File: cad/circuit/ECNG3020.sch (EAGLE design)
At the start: 30 parts, among them Q1 16Mhz, T1 2N3904, T2 2N3904, T3 2N3904, T4 2N3904, T5 2N3904, U1 ATMEGA328P-PU, X1 22-23-2021, X2 22-23-2021, X3 22-23-2021, X4 22-23-2021, X5 22-23-2021, X6 22-23-2021, X7 22-23-2021

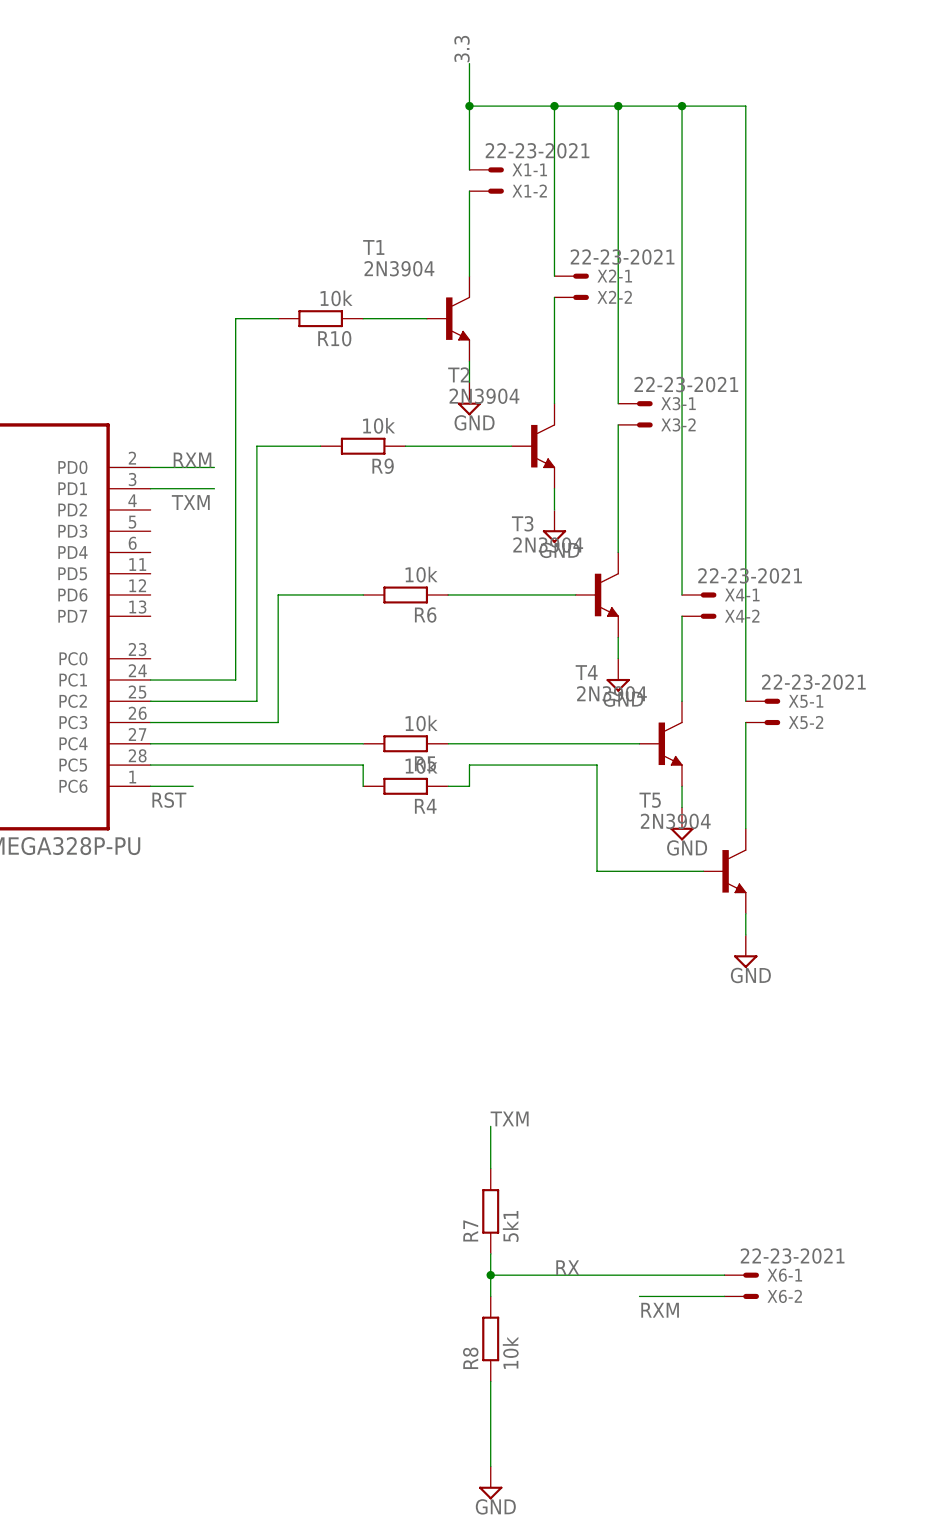
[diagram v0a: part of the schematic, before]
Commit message: Updated the PCB to use I2C instead of UART
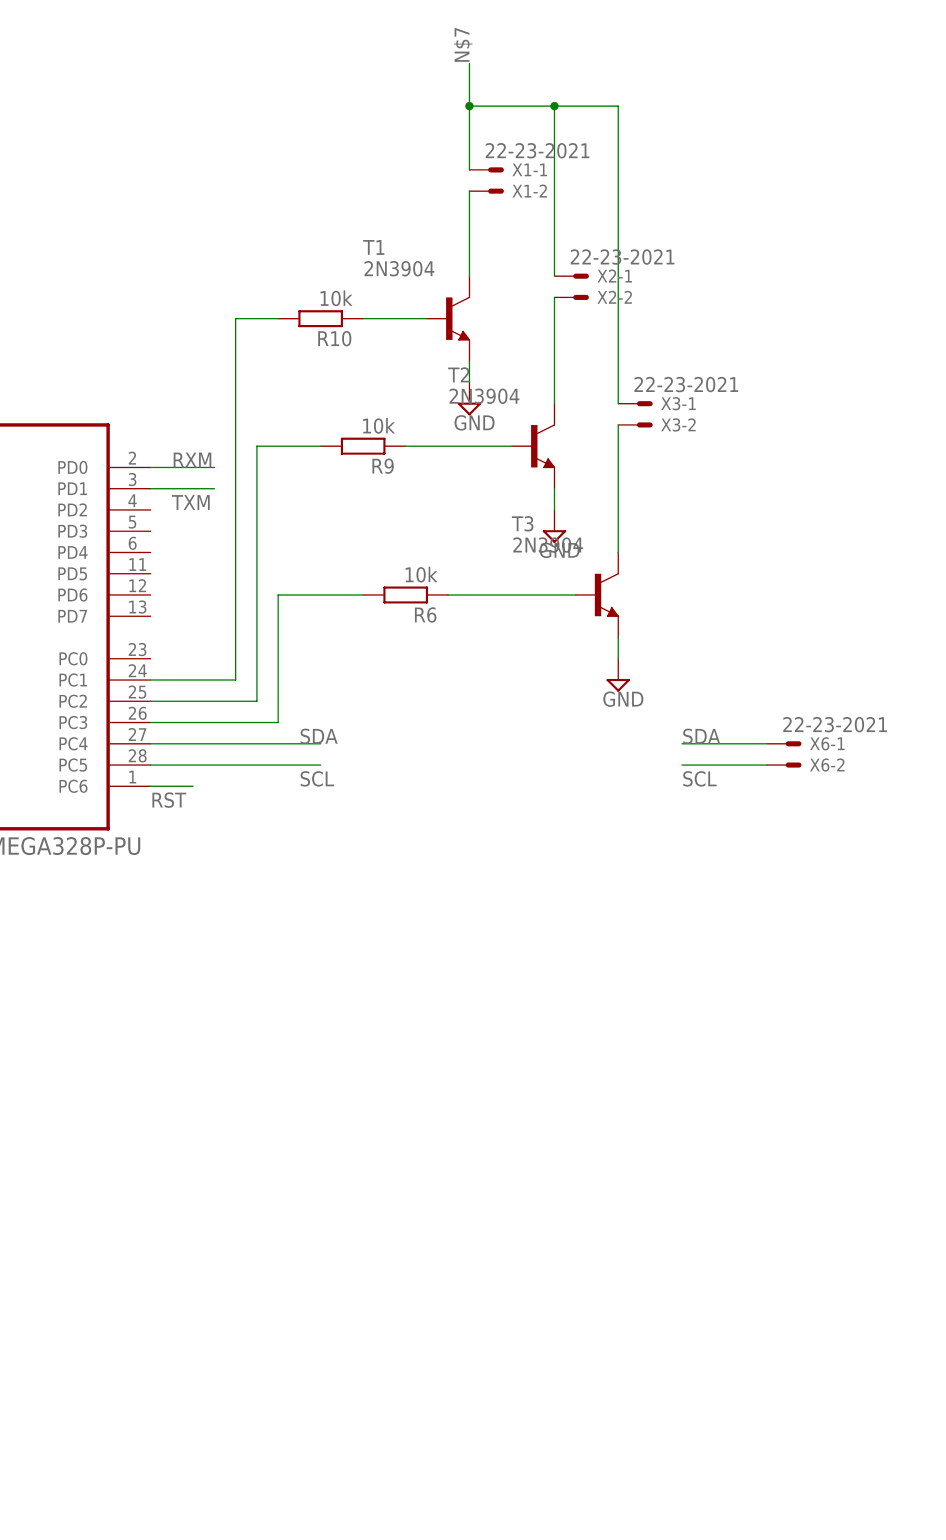
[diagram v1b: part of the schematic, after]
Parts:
- removed R4, R5, R8: 10k, rcl:R-EU_0207/10
- removed R7: 5k1, rcl:R-EU_0207/10
- removed T4, T5: 2N3904, transistor-neu-to92:2N3904
- removed X4, X5: 22-23-2021, con-molex:22-23-2021
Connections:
- removed net N$16: R5.1, T4.B
- removed net N$17: R5.2, U1.PC4
- removed net N$18: R4.2, U1.PC5
- removed net N$8: T5.C, X5-2.S
- removed net N$9: T4.C, X4-2.S
- removed net RX: R7.1, R8.2, X6-1.S
- new net SCL: U1.PC5, X6-2.S
- new net SDA: U1.PC4, X6-1.S
- net 3.3: no longer X1-1.S, X2-1.S, X3-1.S, X4-1.S, X5-1.S
- net GND: no longer R8.1, T4.E, T5.E
- net N$7: now also X1-1.S, X2-1.S, X3-1.S; no longer R4.1, T5.B
- net RXM: no longer X6-2.S
- net TXM: no longer R7.2
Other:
- moved on the sheet: X6-1, X6-2

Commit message: Updated the schematic and board
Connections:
- removed net RXM: U1.PD0
- removed net TXM: U1.PD1
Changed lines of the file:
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@@
-</segment>
-</net>
-<net name="TXM" class="0">
-<segment>
-<pinref part="U1" gate="A" pin="PD1"/>
-<wire x1="50.8" y1="104.14" x2="58.42" y2="104.14" width="0.1524" layer="91"/>
-<label x="53.34" y="101.6" size="1.778" layer="95"/>
-</segment>
-</net>
-<net name="RXM" class="0">
-<segment>
-<pinref part="U1" gate="A" pin="PD0"/>
-<wire x1="50.8" y1="106.68" x2="58.42" y2="106.68" width="0.1524" layer="91"/>
-<label x="53.34" y="106.68" size="1.778" layer="95"/>
 </segment>
 </net>

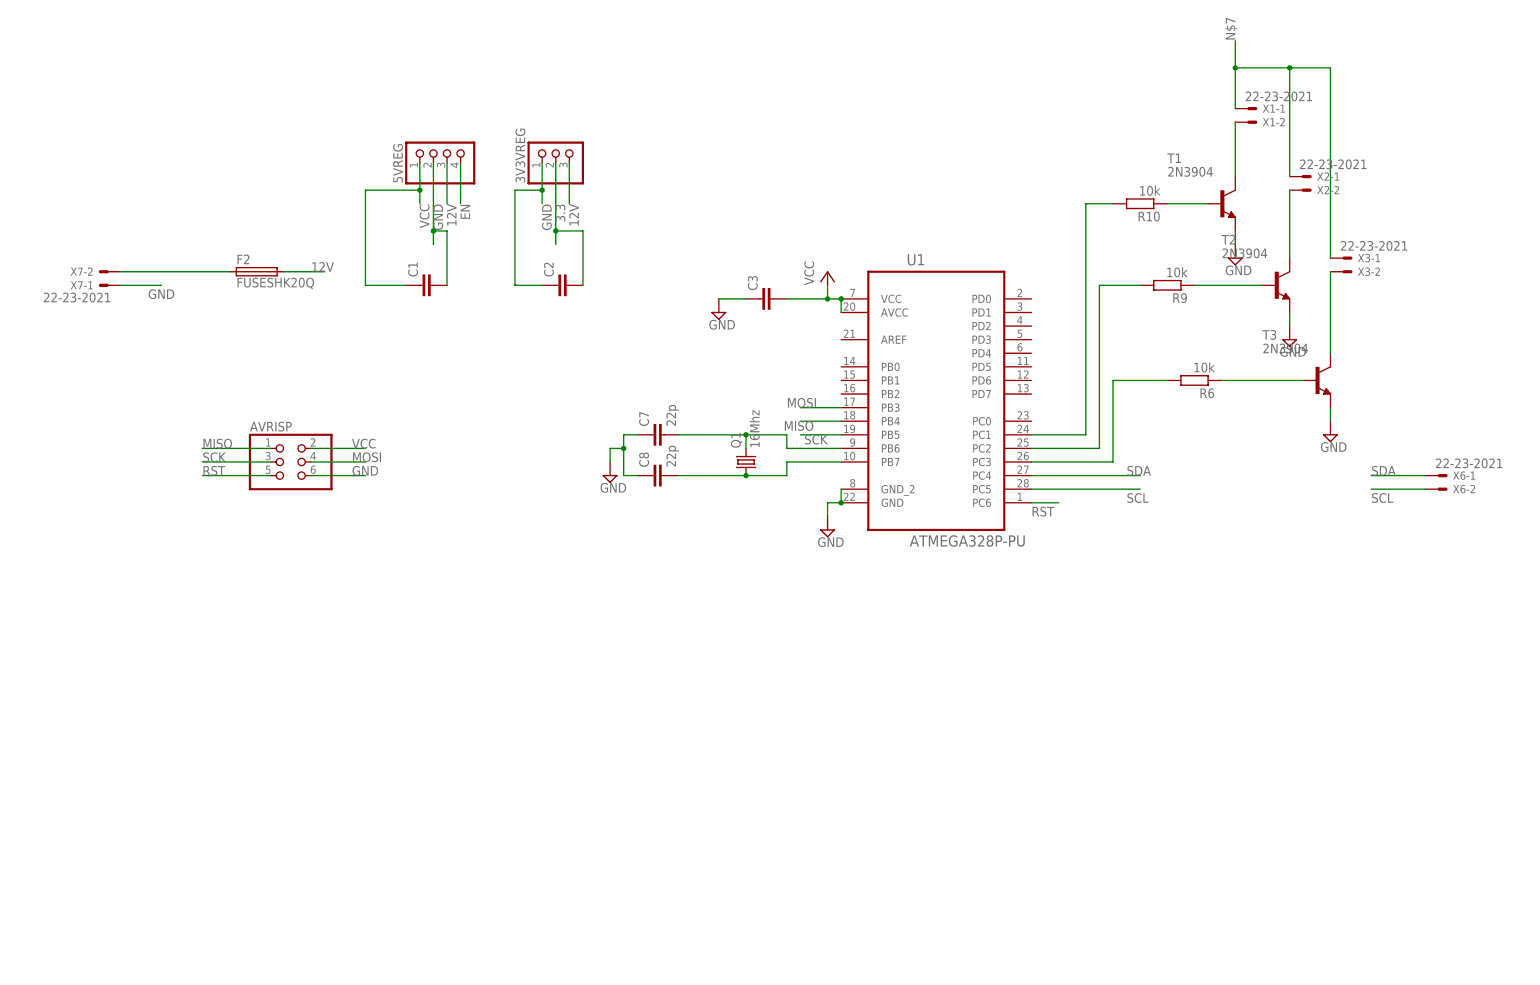
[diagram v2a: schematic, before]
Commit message: Added in rpi power source
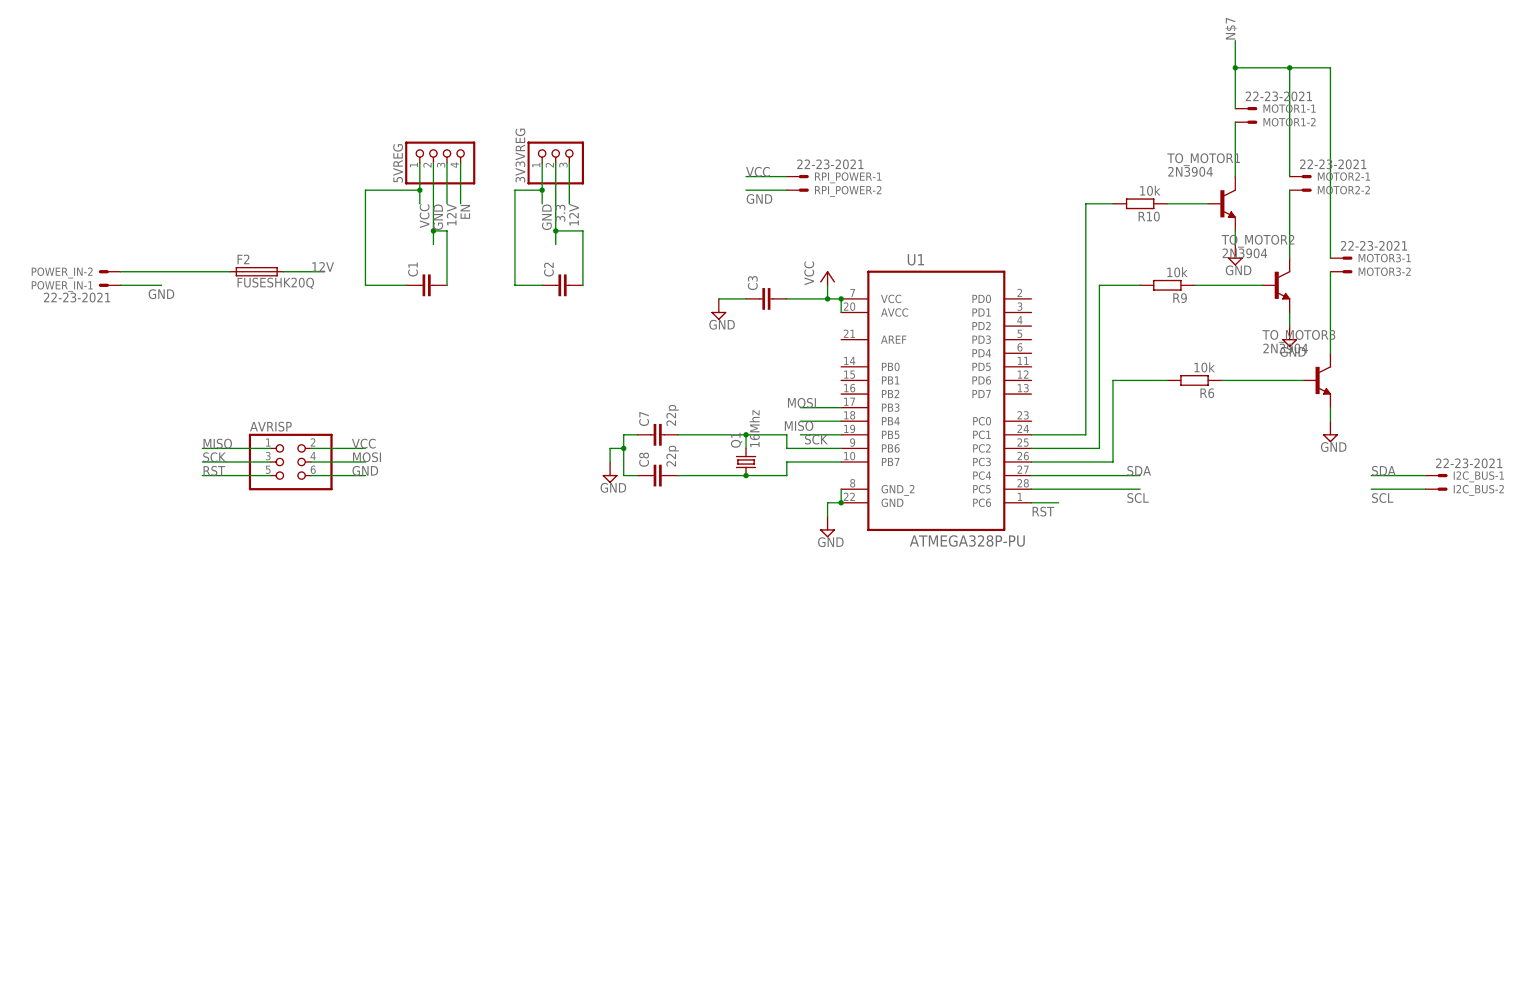
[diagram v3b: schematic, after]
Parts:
- added RPI_POWER: 22-23-2021, con-molex:22-23-2021
- renumbered T1 to TO_MOTOR1, T2 to TO_MOTOR2, T3 to TO_MOTOR3, X1 to MOTOR1, X2 to MOTOR2, X3 to MOTOR3, X6 to I2C_BUS, X7 to POWER_IN
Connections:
- net GND: now also RPI_POWER-2.S
- net VCC: now also RPI_POWER-1.S

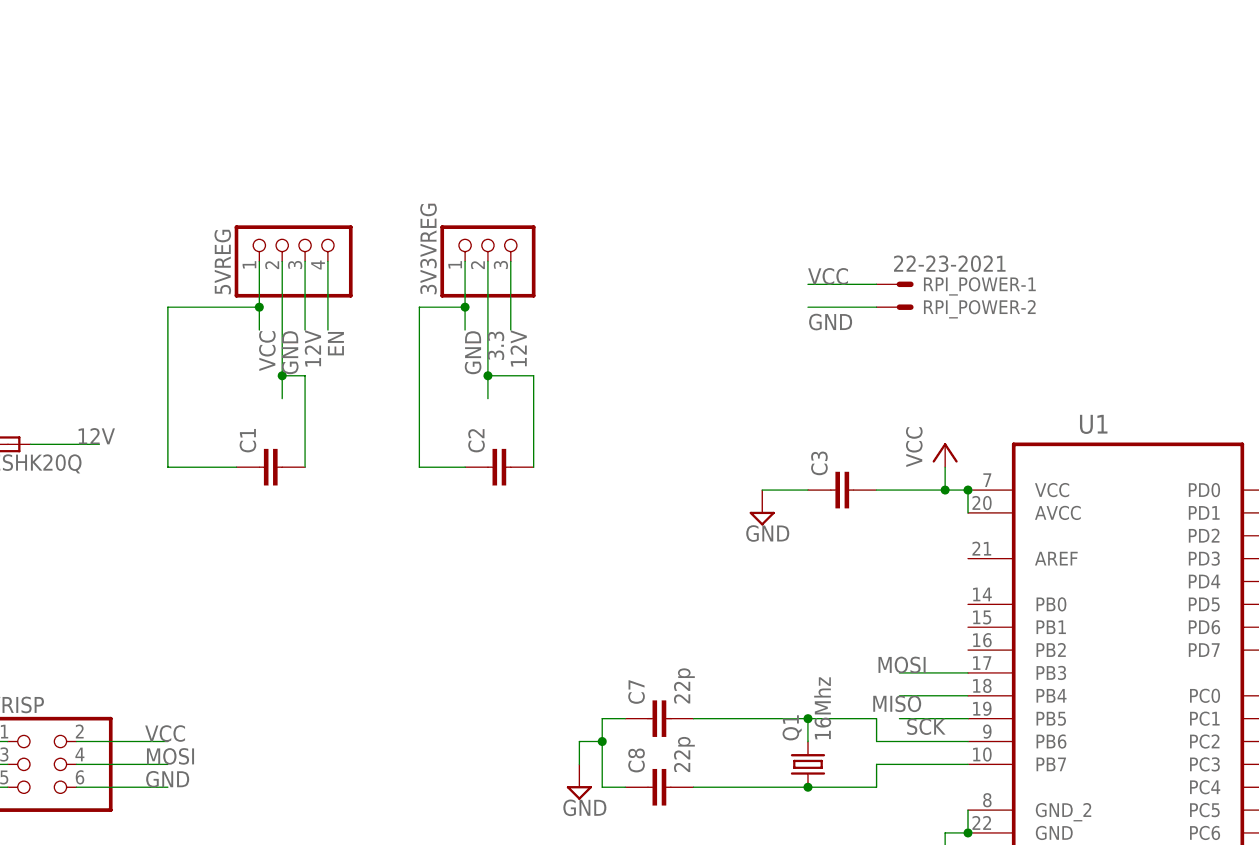
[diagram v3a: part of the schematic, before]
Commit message: Put 2 5V bucks in parallel to increase current to rpi
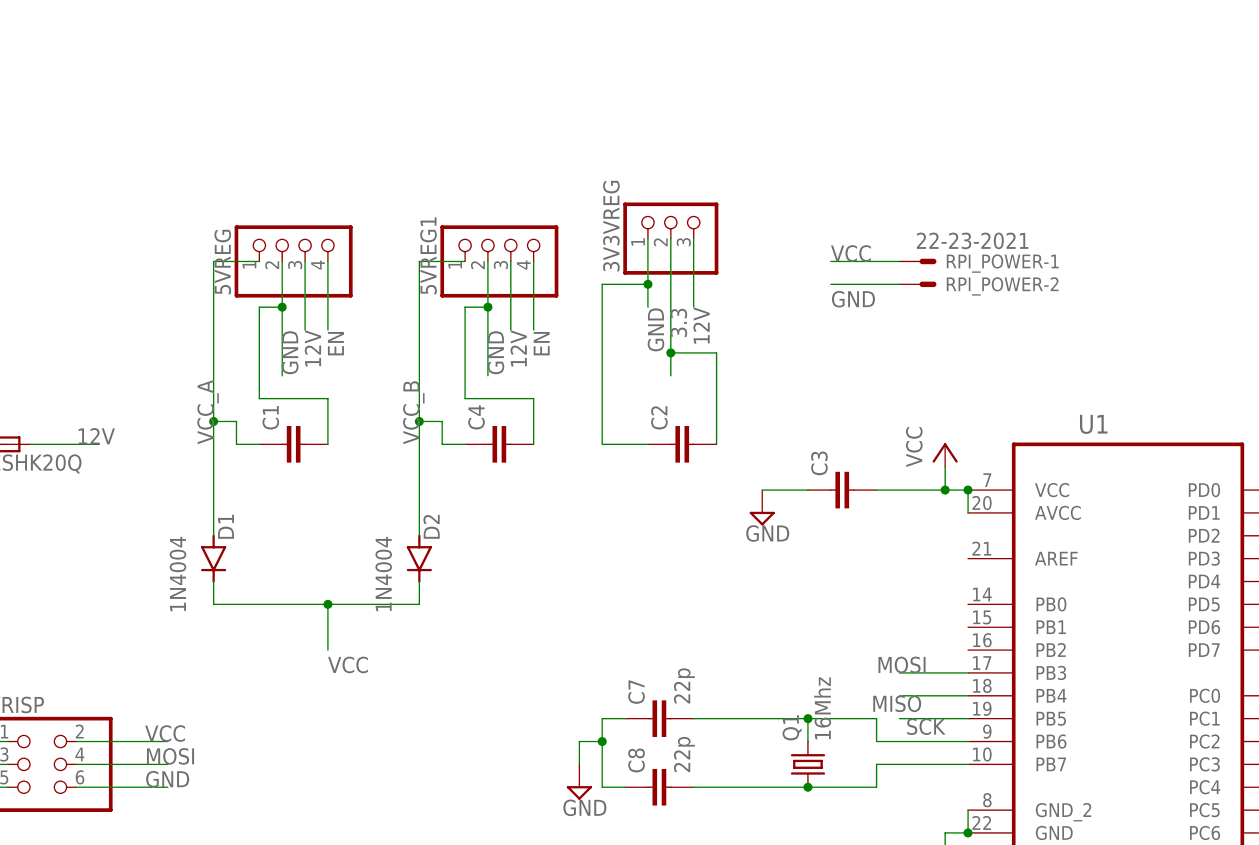
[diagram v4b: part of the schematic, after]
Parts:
- added 5VREG1: (no value), pinhead_2:PINHD-1X4M
- added C4: (no value), capacitor-wima:C2,5-3
- added D1, D2: 1N4004, diode:1N4004
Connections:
- new net VCC_A: 5VREG.1, C1.1, D1.A
- new net VCC_B: 5VREG1.1, C4.1, D2.A
- net 12V: now also 5VREG1.3
- net EN: now also 5VREG1.4
- net GND: now also 5VREG1.2, C4.2
- net VCC: now also D1.C, D2.C; no longer 5VREG.1, C1.1
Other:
- moved on the sheet: 3V3VREG, C1, C2, RPI_POWER-1, RPI_POWER-2
